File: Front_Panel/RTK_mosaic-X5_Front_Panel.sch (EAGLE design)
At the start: 11 parts

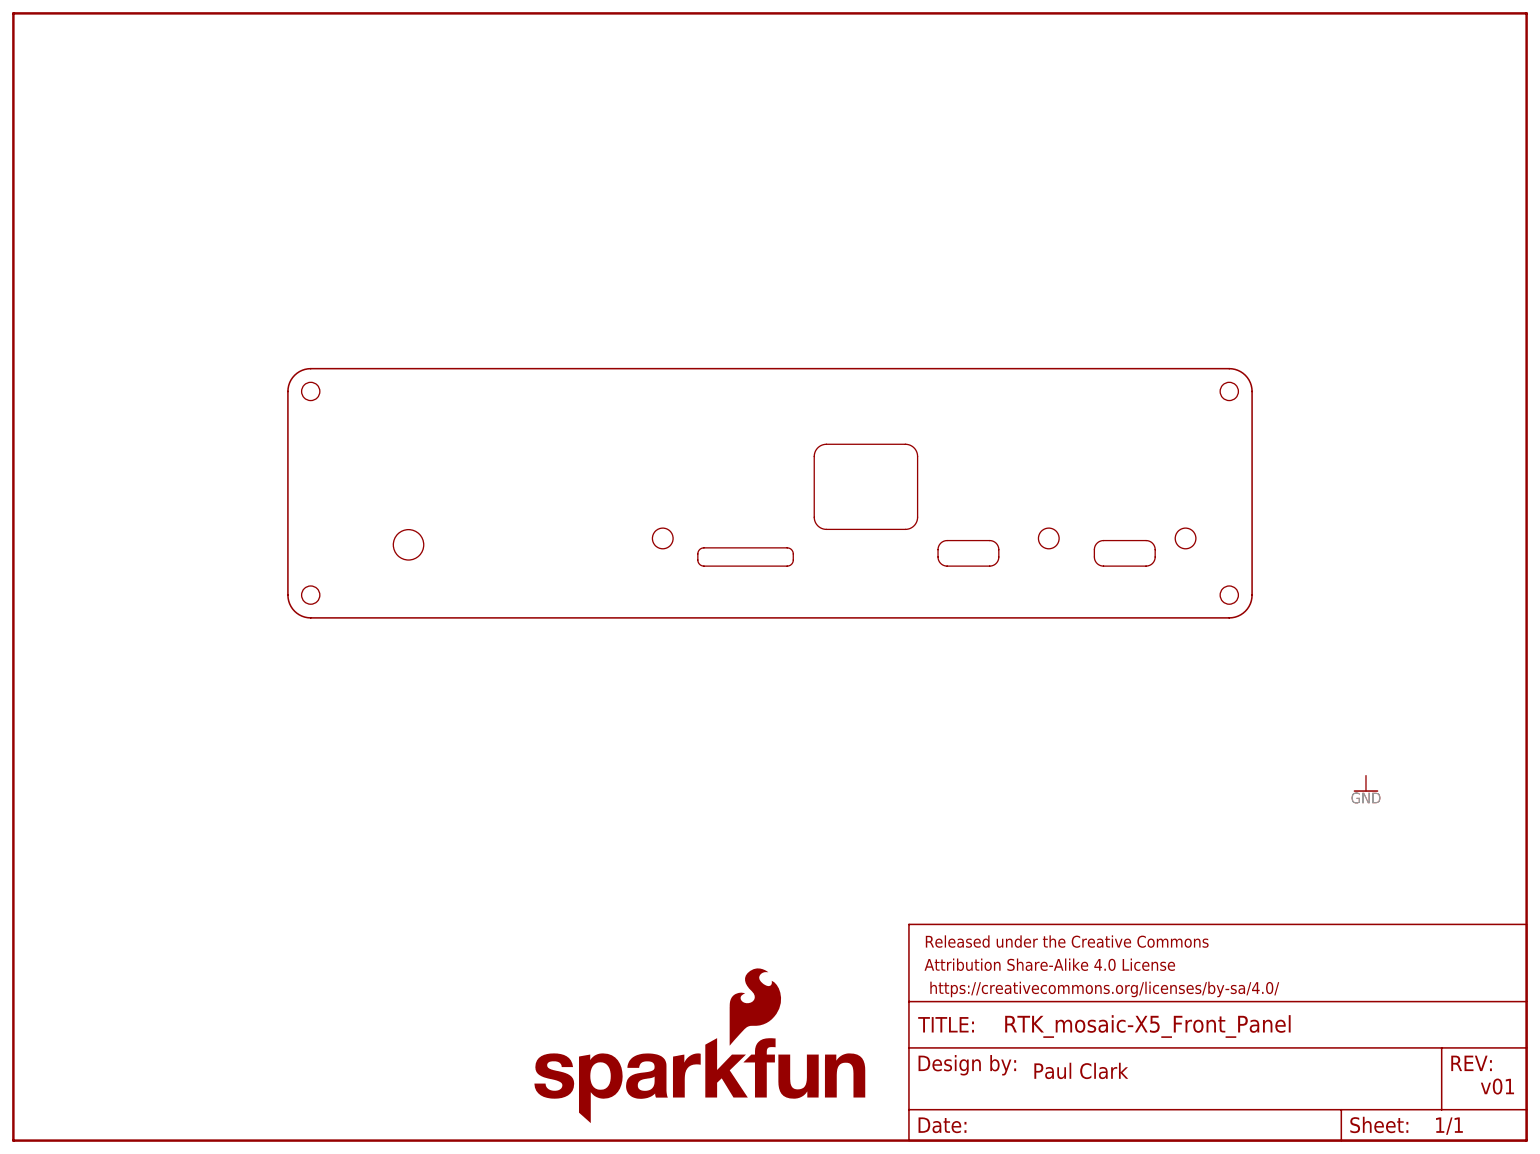
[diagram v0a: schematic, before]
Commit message: Update front panel with new 1.3" OLED
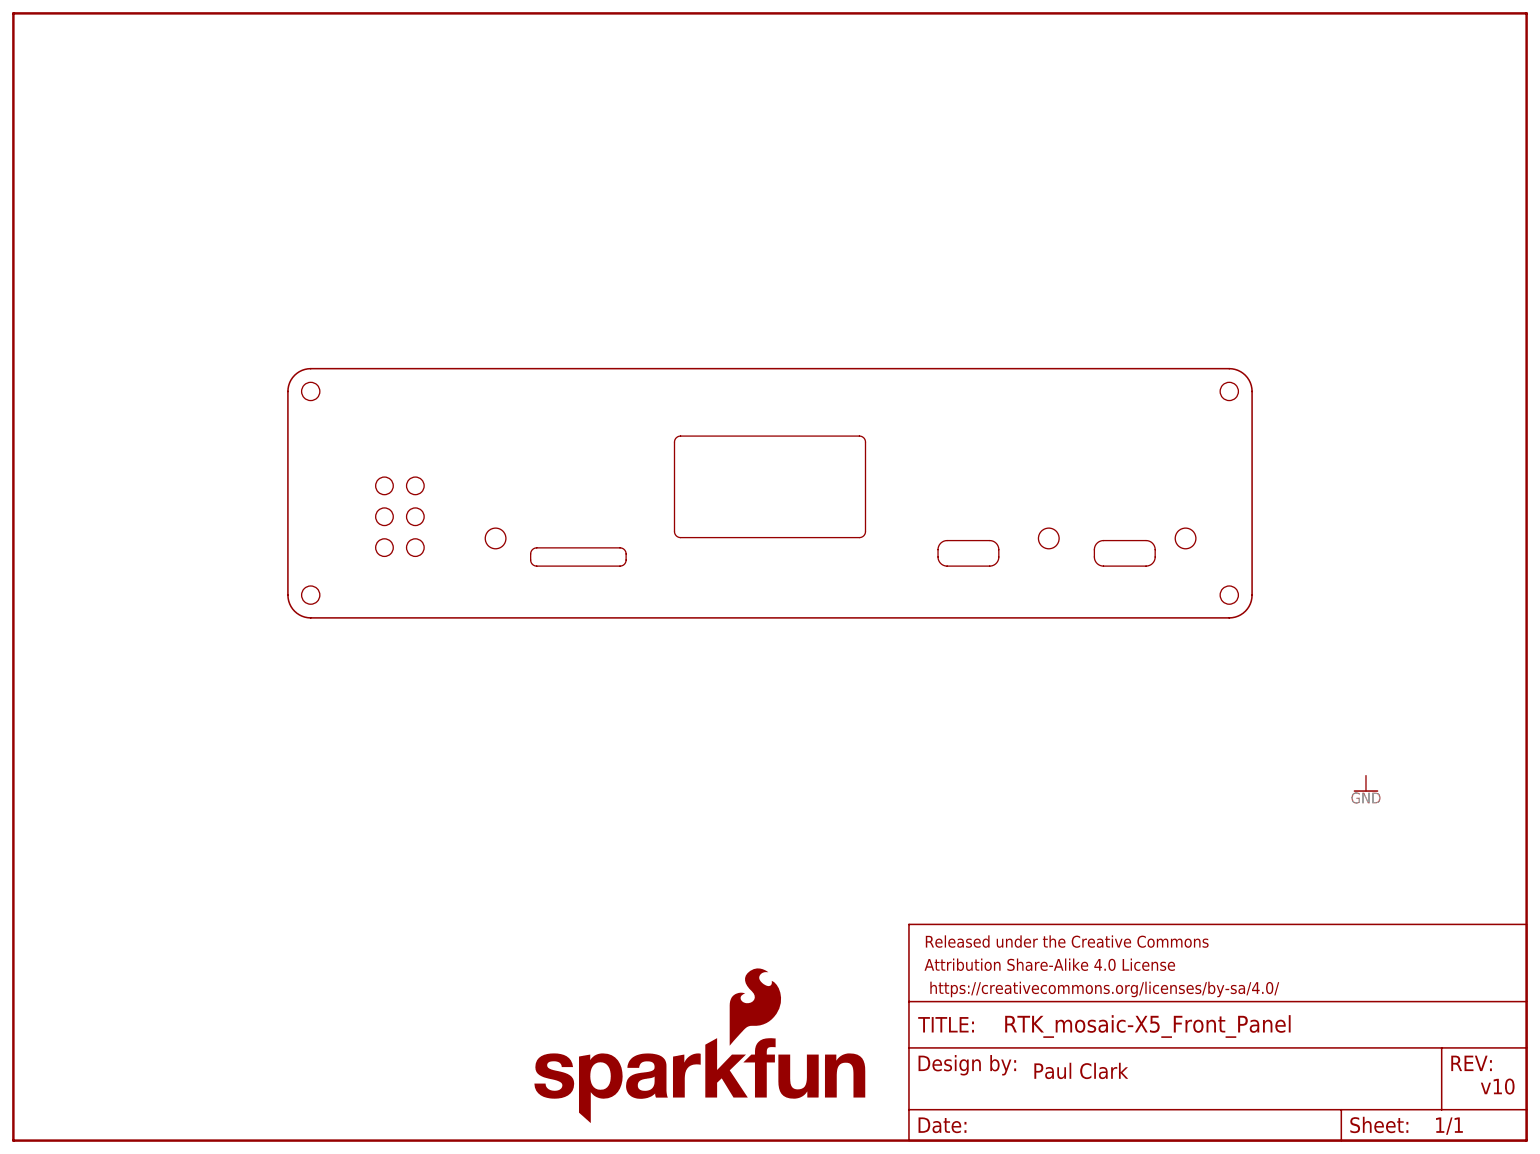
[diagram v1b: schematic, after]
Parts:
- removed LED: LED_DIO-13847, SparkFun-Enclosure-Panel:LED_DIO-13847
- added U$16, U$5: CBI_LED_TRIPLE-3MM_DIO-19990, SparkFun-Enclosure-Panel:CBI_LED_TRIPLE-3MM_DIO-19990
- OLED: value OLED_14532 -> OLED_1.3_128X64; device SparkFun-Enclosure-Panel:OLED_14532 -> SparkFun-Enclosure-Panel:OLED_1.3_128X64
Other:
- note added: "v10"
- note removed: "v01"
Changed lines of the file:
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@@
 <setting verticaltext="up"/>
 </settings>
-<grid distance="0.1" unitdist="inch" unit="inch" style="lines" multiple="1" display="no" altdistance="0.01" altunitdist="inch" altunit="inch"/>
+<grid distance="2.5" unitdist="mm" unit="mm" style="lines" multiple="1" display="no" altdistance="0.5" altunitdist="mm" altunit="mm"/>
 <layers>
 <layer number="1" name="Top" color="4" fill="1" visible="no" active="no"/>
@@
 <part name="PANEL_OUTLINE" library="SparkFun-Enclosure-Panel" deviceset="PANEL_OUTLINE" device=""/>
 <part name="GND1" library="SparkFun-PowerSymbols" deviceset="GND" device=""/>
-<part name="LED" library="SparkFun-Enclosure-Panel" deviceset="LED_DIO-13847" device=""/>
 <part name="RESET" library="SparkFun-Enclosure-Panel" deviceset="BUTTON_SWCH-13896" device=""/>
 <part name="BOOT" library="SparkFun-Enclosure-Panel" deviceset="BUTTON_SWCH-13896" device=""/>
@@
 <part name="ESP32_USB" library="SparkFun-Enclosure-Panel" deviceset="USB-C_CONN-14122" device=""/>
 <part name="GNSS_USB" library="SparkFun-Enclosure-Panel" deviceset="USB-C_CONN-14122" device=""/>
-<part name="OLED" library="SparkFun-Enclosure-Panel" deviceset="OLED_14532" device=""/>
+<part name="OLED" library="SparkFun-Enclosure-Panel" deviceset="OLED_1.3_128X64" device=""/>
 <part name="LOGO1" library="SparkFun-Aesthetics" deviceset="SFE_LOGO_NAME_FLAME" device=".3_INCH" value="SFE_LOGO_NAME_FLAME.3_INCH"/>
 <part name="RESET1" library="SparkFun-Enclosure-Panel" deviceset="BUTTON_SWCH-13896" device=""/>
+<part name="U$5" library="SparkFun-Enclosure-Panel" deviceset="CBI_LED_TRIPLE-3MM_DIO-19990" device=""/>
+<part name="U$16" library="SparkFun-Enclosure-Panel" deviceset="CBI_LED_TRIPLE-3MM_DIO-19990" device=""/>
 </parts>
 <sheets>
 <sheet>
 <plain>
-<text x="241.3" y="7.62" size="2.54" layer="94" font="vector">v01</text>
+<text x="241.3" y="7.62" size="2.54" layer="94" font="vector">v10</text>
 <text x="167.64" y="10.16" size="2.54" layer="94" font="vector">Paul Clark</text>
 </plain>
@@
 <attribute name="VALUE" x="222.5" y="57.246" size="1.778" layer="96" font="vector" align="top-center"/>
 </instance>
-<instance part="LED" gate="G$1" x="65" y="95" smashed="yes"/>
 <instance part="RESET" gate="G$1" x="170.32" y="95" smashed="yes"/>
 <instance part="BOOT" gate="G$1" x="192.82" y="95" smashed="yes"/>
-<instance part="MICRO_SD" gate="G$1" x="120.44" y="95" smashed="yes"/>
+<instance part="MICRO_SD" gate="G$1" x="92.94" y="95" smashed="yes"/>
 <instance part="ESP32_USB" gate="G$1" x="182.82" y="95" smashed="yes"/>
 <instance part="GNSS_USB" gate="G$1" x="157.1" y="95" smashed="yes"/>
-<instance part="OLED" gate="G$1" x="140.24" y="107.54" smashed="yes"/>
+<instance part="OLED" gate="G$1" x="124.46" y="107.54" smashed="yes"/>
 <instance part="LOGO1" gate="G$1" x="85" y="2.5" smashed="yes"/>
-<instance part="RESET1" gate="G$1" x="106.82" y="95" smashed="yes"/>
+<instance part="RESET1" gate="G$1" x="79.32" y="95" smashed="yes"/>
+<instance part="U$5" gate="G$1" x="61.04" y="95" smashed="yes"/>
+<instance part="U$16" gate="G$1" x="66.12" y="95" smashed="yes"/>
 </instances>
 <busses>
